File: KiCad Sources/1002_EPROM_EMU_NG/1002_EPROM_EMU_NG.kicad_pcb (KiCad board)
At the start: 2 copper layers, 99.1 x 88.9 mm, 41 parts, among them J1 IDC34, M1 Arduino Nano v3.0, Q1 BC547, Q2 BC557, SW1 SW_Push, U1 74HC00, U10 74HC541, U11 74HC541, U2 74HC08, U3 25LC512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

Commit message: Add files via upload
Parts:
- added TP1: VCC, TestPoint:TestPoint_THTPad_D1.5mm_Drill0.7mm, F.Cu at (115.7, 112.5)
- added TP2: GND, TestPoint:TestPoint_THTPad_D1.5mm_Drill0.7mm, F.Cu at (133.5, 134.4)
- added TP3: GND, TestPoint:TestPoint_THTPad_D1.5mm_Drill0.7mm, F.Cu at (129.2, 134.4)
- moved REF** 2.54 mm to (198.0, 59.7)
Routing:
- net VCC: track 417.2 -> 439.9 mm
- net GND: track 450.5 -> 464.1 mm
- net /EN_A12: track 56.6 -> 47.5 mm, vias 0 -> 1
- net /~RESET~: track 132.9 -> 139.1 mm
- net /SS: track 21.4 -> 24.5 mm
- net /D7: track 94.3 -> 91.5 mm
- net /RESET: track 126.4 -> 129.2 mm
- net /D6: track 100.2 -> 98.1 mm
- net /A15: track 66.4 -> 67.8 mm
- net /DATA_LD: track 102.8 -> 104.2 mm
- net /~CS1~: track 79.8 -> 81.0 mm
- net /LD_BTN: track 37.7 -> 38.9 mm
- net /SCLK: track 114.3 -> 115.5 mm
- net /~WE~: track 118.0 -> 116.9 mm, vias 0 -> 1
- net /EN_A13: track 55.1 -> 54.2 mm
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- removed copper zone on B.Cu, net GND
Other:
- board text added: "GND"
- board text added: "Jacob"
- board text added: "Kris Sekula - 2020"
- board text added: "Load"
- board text added: "Power"
- board text added: "RUN"
- board text added: "Sophie"
- board text added: "U1"
- board text added: "U10"
- board text added: "U11"
- board text added: "U2"
- board text added: "U3"
- board text added: "U4"
- board text added: "U5"
- board text added: "U6"
- board text added: "U9"
- board text added: "VCC @ 5V"
- board text added: "v1.3_June-2020"
- board text removed: "Jacob & Sophie"
- board text removed: "Kris Sekula 2020"
- board text removed: "v1.2_June-2020"

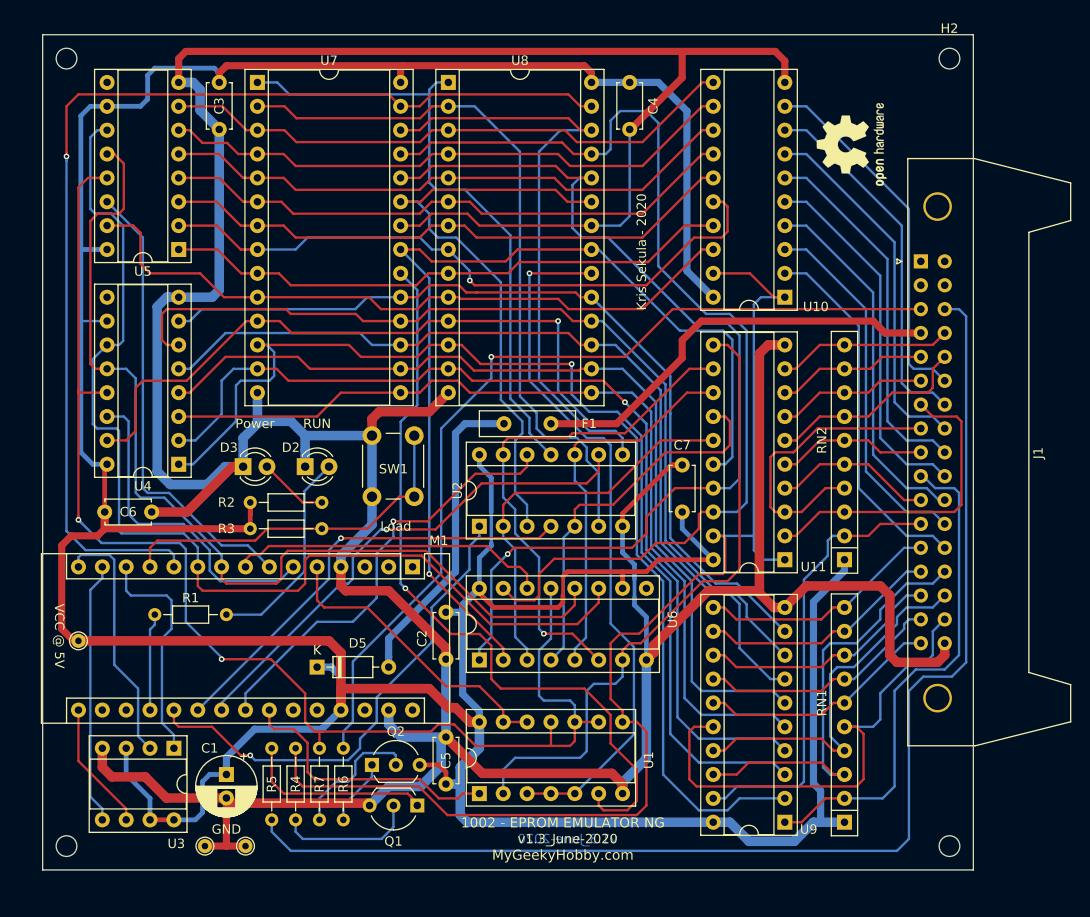
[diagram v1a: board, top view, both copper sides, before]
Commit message: Version 1.4 of PCB, with optimised power routing.
Hopefully this will fix the CMOS latch-up I was getting on U11
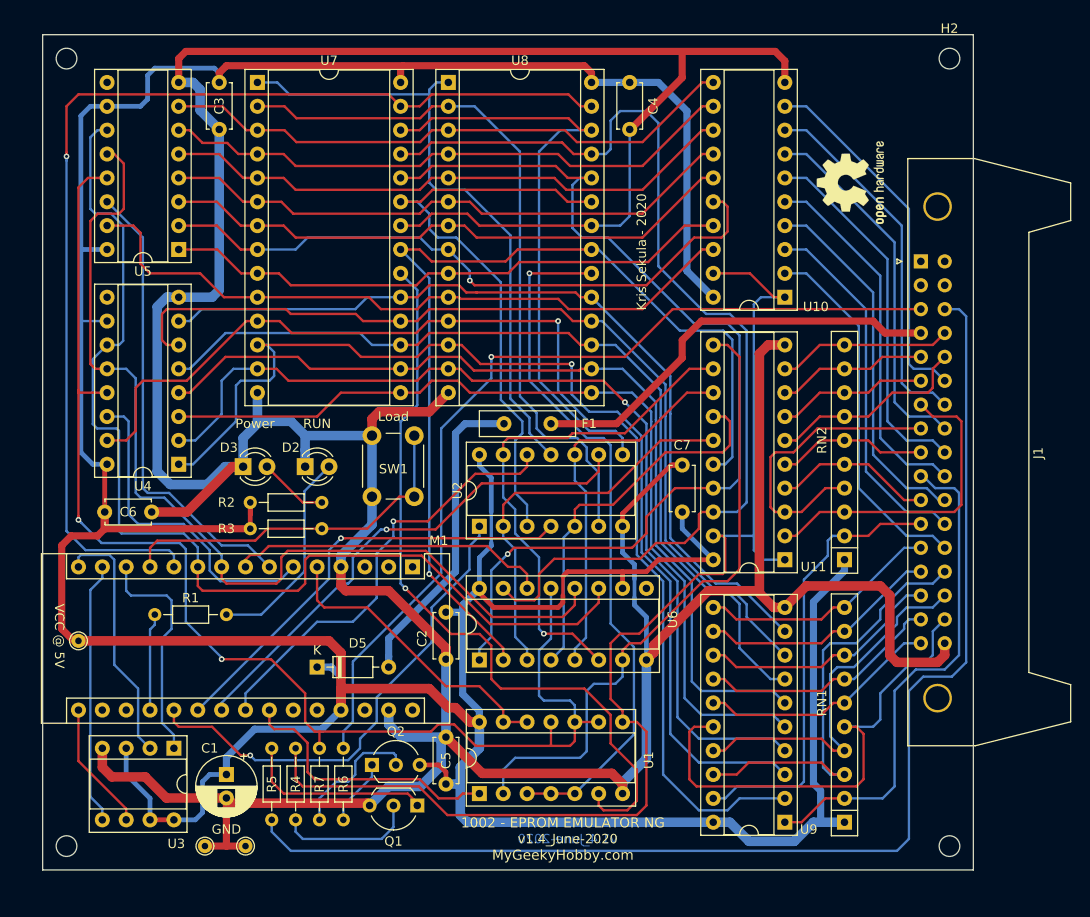
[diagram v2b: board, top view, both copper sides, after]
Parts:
- moved REF** 4.06 mm to (198.0, 63.8)
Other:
- board text added: "v1.4_June-2020"
- board text removed: "v1.3_June-2020"
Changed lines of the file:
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@@
       (viasonmask false)
       (mode 1)
-      (useauxorigin true)
+      (useauxorigin false)
       (hpglpennumber 1)
       (hpglpenspeed 20)
@@
       (drillshape 0)
       (scaleselection 1)
-      (outputdirectory "Gerbers_1.3_PCBWAY/"))
+      (outputdirectory "Gerbers_1.4/"))
   )
   (net 0 "")
@@
   )
   (module Symbol:OSHW-Logo2_9.8x8mm_SilkScreen (layer F.Cu)
-    (at 197.993 59.69 90)
+    (at 197.993 63.754 90)
     (descr "Open Source Hardware Symbol")
     (tags "Logo Symbol OSHW")
@@
     )
   )
-  (gr_text v1.3_June-2020 (at 167.767 133.604) (layer B.Cu)
+  (gr_text v1.4_June-2020 (at 167.767 133.604) (layer B.Cu)
     (effects (font (size 1 1) (thickness 0.15)) (justify mirror))
   )
@@
     (effects (font (size 1 1) (thickness 0.15)) (justify mirror))
   )
-  (gr_text Load (at 149.479 100.33) (layer F.SilkS)
+  (gr_text Load (at 149.225 88.646) (layer F.SilkS)
     (effects (font (size 1 1) (thickness 0.15)))
   )
@@
     (effects (font (size 1 1) (thickness 0.15)))
   )
-  (gr_text v1.3_June-2020 (at 167.767 133.604) (layer F.SilkS)
+  (gr_text v1.4_June-2020 (at 167.767 133.604) (layer F.SilkS)
     (effects (font (size 1 1) (thickness 0.15)))
   )

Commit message: Updated PCB to version 1.6
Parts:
- removed REF**: OSHW-Logo2_9.8x8mm_SilkScreen, Symbol:OSHW-Logo2_9.8x8mm_SilkScreen
- added H5: MountingHole, Symbol:OSHW-Logo2_9.8x8mm_SilkScreen, F.Cu at (198.2, 63.2)
- added TP4: VCC, TestPoint:TestPoint_THTPad_D1.5mm_Drill0.7mm, F.Cu at (115.7, 114.6)
- C1: value 100uF -> 10uF
- Q1: value BC547 -> 2N4401
- Q2: value BC557 -> 2N4403
- R4: value 10k -> 4k7
- U10, U11, U9: value 74HC541 -> 74HCT541
- moved C2 27.3 mm to (180.0, 98.8), turned to 90 degrees
- moved C7 27.3 mm to (154.8, 109.5), turned to 270 degrees
- moved TP1 2.29 mm to (115.7, 110.2)
- moved TP2 0.80 mm to (134.2, 134.6)
- moved TP3 0.80 mm to (129.9, 134.6)
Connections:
- J1 pad 1: (no net) -> /E_RESET
- J1 pad 2: (no net) -> /~E_RESET~
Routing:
- net /~E_RESET~: track 133.0 -> 140.5 mm
- net /E_RESET: track 96.0 -> 102.8 mm
- net VCC: track 439.9 -> 443.3 mm
- net /~RESET~: track 139.1 -> 141.0 mm
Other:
- board text added: "+"
- board text added: "1002 - EPROM EMULATOR NG v1.6a_Sep-2020"
- board text added: "<-"
- board text added: "Green"
- board text added: "MyGeekyHobby.com"
- board text added: "Red"
- board text added: "VCC"
- board text added: "v1.6a_Sep-2020"
- board text removed: "1002 - EPROM EMULATOR NG MyGeekyHobby.com"
- board text removed: "VCC @ 5V"
- board text removed: "v1.4_June-2020"
